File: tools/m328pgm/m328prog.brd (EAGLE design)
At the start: 58.1 x 26.7 mm, 11 parts, among them J1 AVR_SPI_PROG_3X2PTH, U1 ATMEGA328P

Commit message: Update several tool boards.
+ AEPRO had the wrong socket size; the ZIF footprint was for
  a narrow 28-pin DIP.
+ AEPRO was missing an inverter on the LEDs.
+ M328PGM had a serial line tied to RST: any attempt at using the
  UART caused the board to reset.
+ M1284PGM had no silkscreen markings to identify the board.
+ M1284PGM had no decoupling capacitor for the MCU.
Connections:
- net N$10: now also CN1.4; no longer CN1.6
- net N$4: now also CN1.6
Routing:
- net N$4: track 67.6 -> 80.4 mm
- net N$10: track 44.9 -> 42.8 mm
- net VCC: track 85.8 -> 87.1 mm
- net GND: track 65.5 -> 64.2 mm
- net N$9: track 47.4 -> 46.3 mm
- net N$8: track 18.0 -> 17.0 mm
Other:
- board text added: "ICSP"
- board text added: "PD2"
- board text added: "REV1/2019-09-30"
- board text removed: "(PD2/2)"
- board text removed: "LED"
- board text removed: "REV0/2019-08-29"

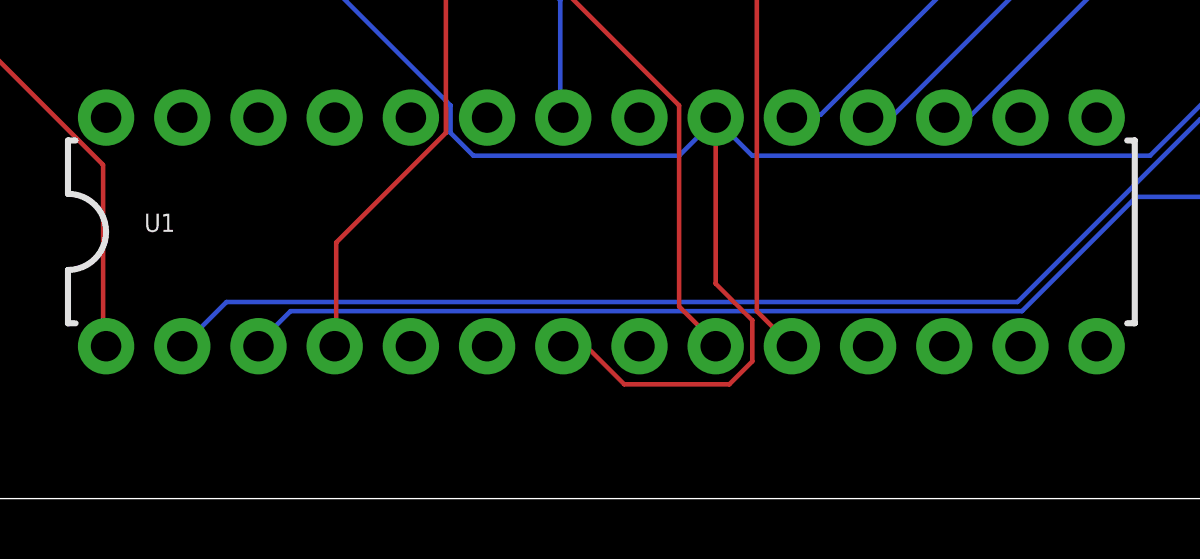
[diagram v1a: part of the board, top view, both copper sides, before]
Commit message: Fix UART issues in programmers.
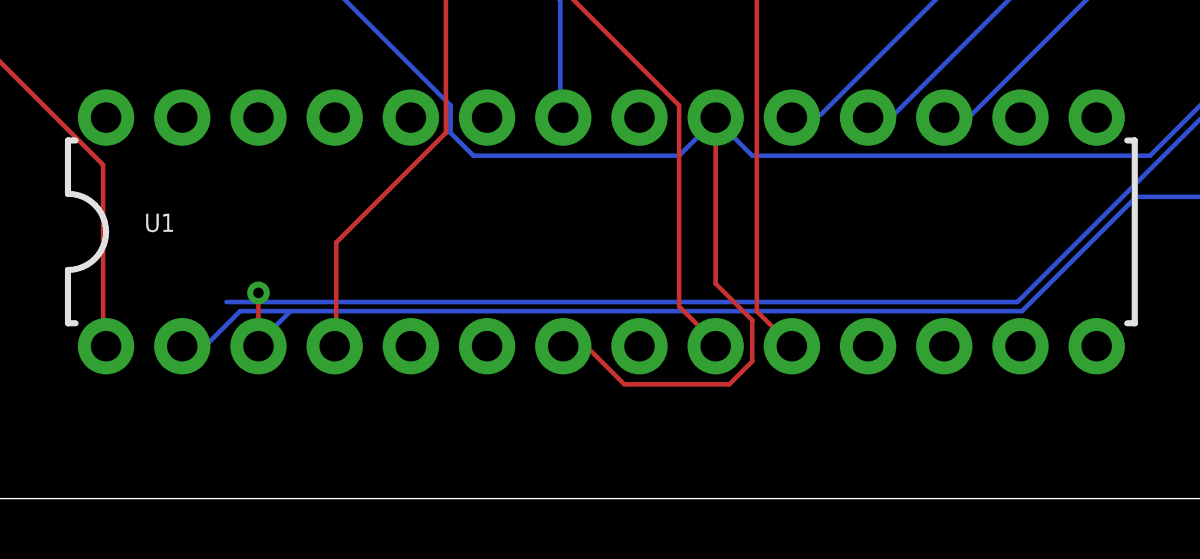
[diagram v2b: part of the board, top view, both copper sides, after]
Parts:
- added FRAME1: FRAME-LETTER, SparkFun-Aesthetics:CREATIVE_COMMONS
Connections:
- net N$10: now also U1.2; no longer U1.3
- net N$9: now also U1.3; no longer U1.2
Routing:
- net N$10: track 42.8 -> 46.8 mm
- net N$9: vias 0 -> 1
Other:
- board text added: "REV2/2019-10-02"
- board text removed: "REV1/2019-09-30"
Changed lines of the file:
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@@
 <drawing>
 <settings>
-<setting alwaysvectorfont="no"/>
+<setting alwaysvectorfont="yes"/>
 <setting verticaltext="up"/>
 </settings>
@@
 <text x="21.59" y="2.54" size="1.016" layer="22" font="vector" rot="MR0" align="center">WNTRMUTE</text>
 <text x="50.8" y="8.89" size="1.016" layer="22" font="vector" rot="MR270" align="center">K. ISOM / OAK CA</text>
-<text x="49.022" y="8.89" size="1.016" layer="22" font="vector" rot="MR270" align="center">REV1/2019-09-30</text>
+<text x="49.022" y="8.89" size="1.016" layer="22" font="vector" rot="MR270" align="center">REV2/2019-10-02</text>
 <text x="54.229" y="2.667" size="1.016" layer="21" font="vector" rot="R90" align="center">GND</text>
 <text x="53.975" y="7.874" size="1.016" layer="21" font="vector" rot="R90" align="center">FTDI</text>
@@
 <attribute name="VALUE" x="27.559" y="21.59" size="0.6096" layer="27" font="vector" ratio="20" rot="R90" align="top-center"/>
 </element>
+<element name="FRAME1" library="SparkFun-Aesthetics" package="CREATIVE_COMMONS" value="FRAME-LETTER" x="11.43" y="-8.89" smashed="yes">
+<attribute name="DESIGNER" value="K. ISOM" x="11.43" y="-8.89" size="1.778" layer="27" display="off"/>
+<attribute name="REV" value="1" x="11.43" y="-8.89" size="1.778" layer="27" display="off"/>
+</element>
 </elements>
 <signals>
@@
 </signal>
 <signal name="N$9">
-<contactref element="U1" pad="2"/>
 <contactref element="CN1" pad="5"/>
 <wire x1="46.6344" y1="12.6492" x2="55.7784" y2="12.6492" width="0.1524" layer="16"/>
 <wire x1="40.5384" y1="6.5532" x2="46.6344" y2="12.6492" width="0.1524" layer="16"/>
-<wire x1="14.1732" y1="6.5532" x2="40.5384" y2="6.5532" width="0.1524" layer="16"/>
-<wire x1="12.7" y1="5.08" x2="14.1732" y2="6.5532" width="0.1524" layer="16"/>
+<wire x1="14.1732" y1="6.5532" x2="15.24" y2="6.5532" width="0.1524" layer="16"/>
+<wire x1="15.24" y1="6.5532" x2="40.5384" y2="6.5532" width="0.1524" layer="16"/>
 <wire x1="55.7784" y1="12.6492" x2="55.88" y2="12.7" width="0.1524" layer="16"/>
+<contactref element="U1" pad="3"/>
+<wire x1="15.24" y1="6.858" x2="15.24" y2="5.08" width="0.1524" layer="1"/>
+<wire x1="15.24" y1="6.5532" x2="15.24" y2="6.858" width="0.1524" layer="16"/>
+<via x="15.24" y="6.858" extent="1-16" drill="0.35"/>
 </signal>
 <signal name="N$10">
-<contactref element="U1" pad="3"/>
 <contactref element="CN1" pad="4"/>
 <wire x1="44.5008" y1="10.0584" x2="55.7784" y2="10.0584" width="0.1524" layer="16"/>
@@
 <wire x1="15.24" y1="5.1816" x2="16.3068" y2="6.2484" width="0.1524" layer="16"/>
 <wire x1="55.7784" y1="10.0584" x2="55.88" y2="10.16" width="0.1524" layer="16"/>
-<wire x1="15.24" y1="5.1816" x2="15.24" y2="5.08" width="0.1524" layer="16"/>
+<contactref element="U1" pad="2"/>
+<wire x1="13.5636" y1="5.1816" x2="12.8016" y2="5.1816" width="0.1524" layer="16"/>
+<wire x1="14.6304" y1="6.2484" x2="13.5636" y2="5.1816" width="0.1524" layer="16"/>
+<wire x1="16.3068" y1="6.2484" x2="14.6304" y2="6.2484" width="0.1524" layer="16"/>
+<wire x1="12.8016" y1="5.1816" x2="12.7" y2="5.08" width="0.1524" layer="16"/>
 </signal>
 </signals>
